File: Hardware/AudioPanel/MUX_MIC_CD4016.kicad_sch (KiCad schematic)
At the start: 8 parts, among them U57 ADG729, U58 ADG729

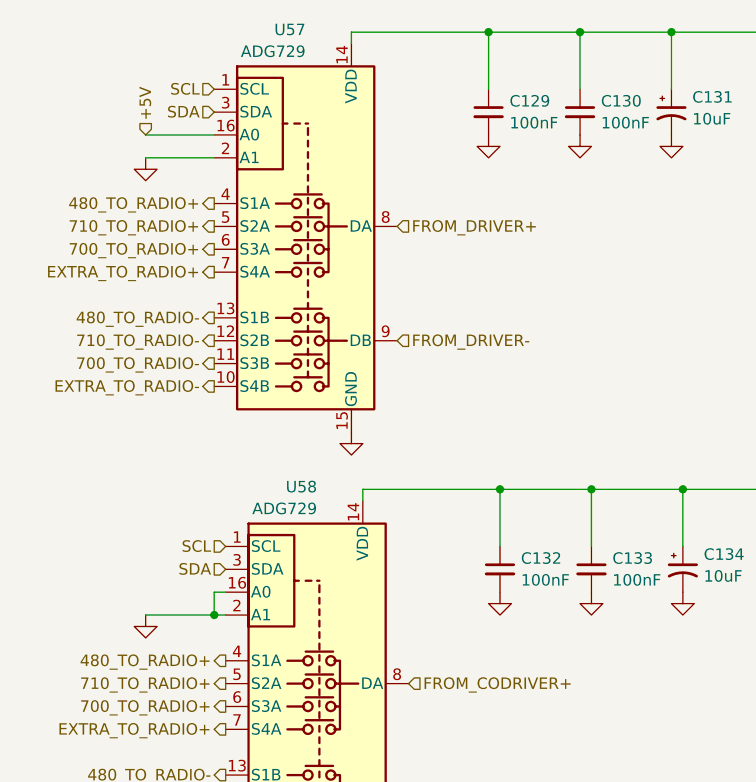
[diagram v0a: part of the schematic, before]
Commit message: Added MIC port protection
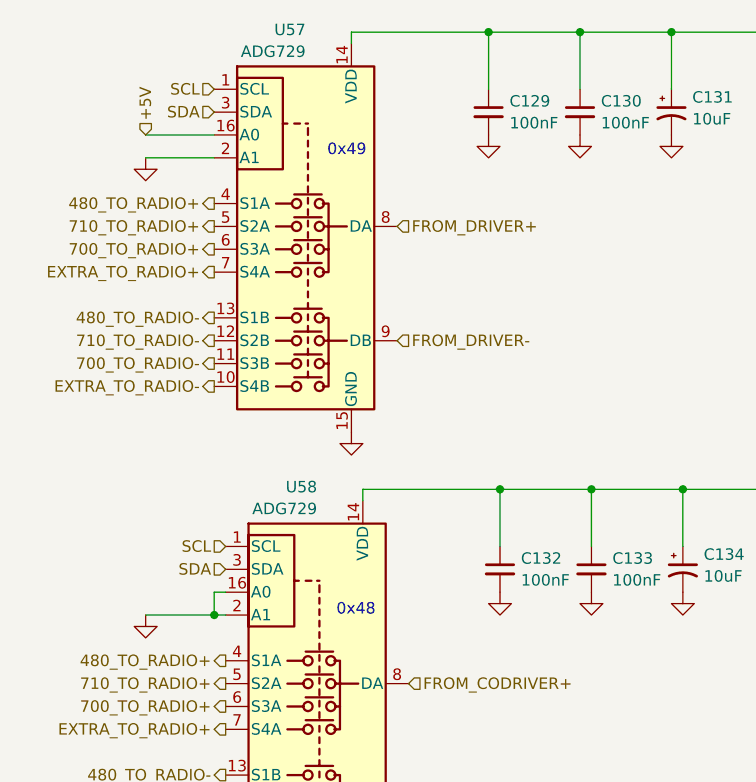
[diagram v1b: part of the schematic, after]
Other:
- note added: "0x48"
- note added: "0x49"
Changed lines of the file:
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@@
 	(generator_version "9.0")
 	(paper "A4")
+	(text "0x48"
+		(exclude_from_sim no)
+		(at 93.218 111.252 0)
+		(effects
+			(font
+				(size 1.27 1.27)
+			)
+		)
+	)
+	(text "0x49"
+		(exclude_from_sim no)
+		(at 92.202 60.198 0)
+		(effects
+			(font
+				(size 1.27 1.27)
+			)
+		)
+	)
 	(junction
 		(at 107.95 46.99)

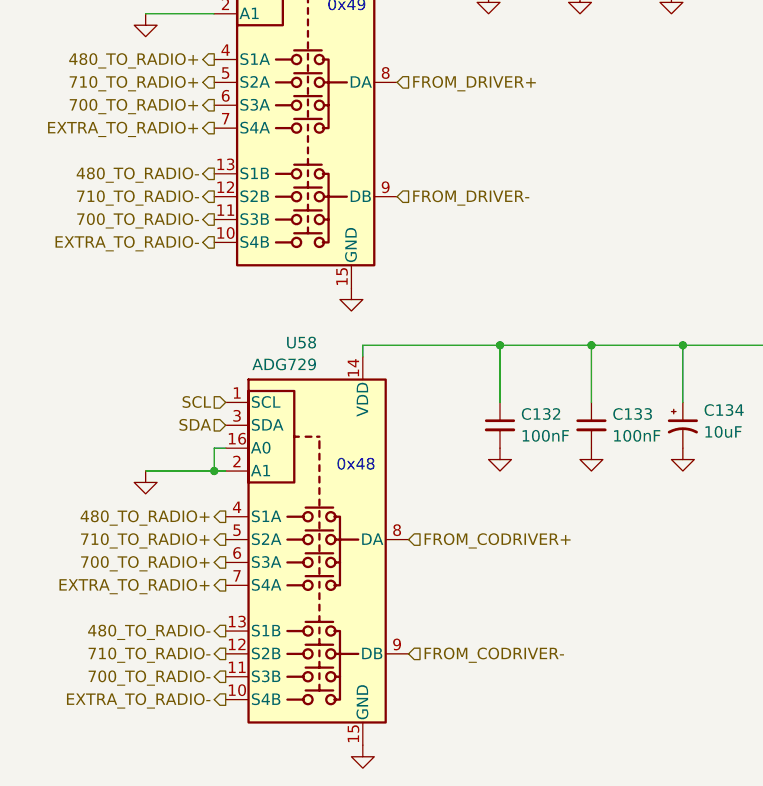
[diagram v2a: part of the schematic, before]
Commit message: Revisiting the audio input buffer circuit
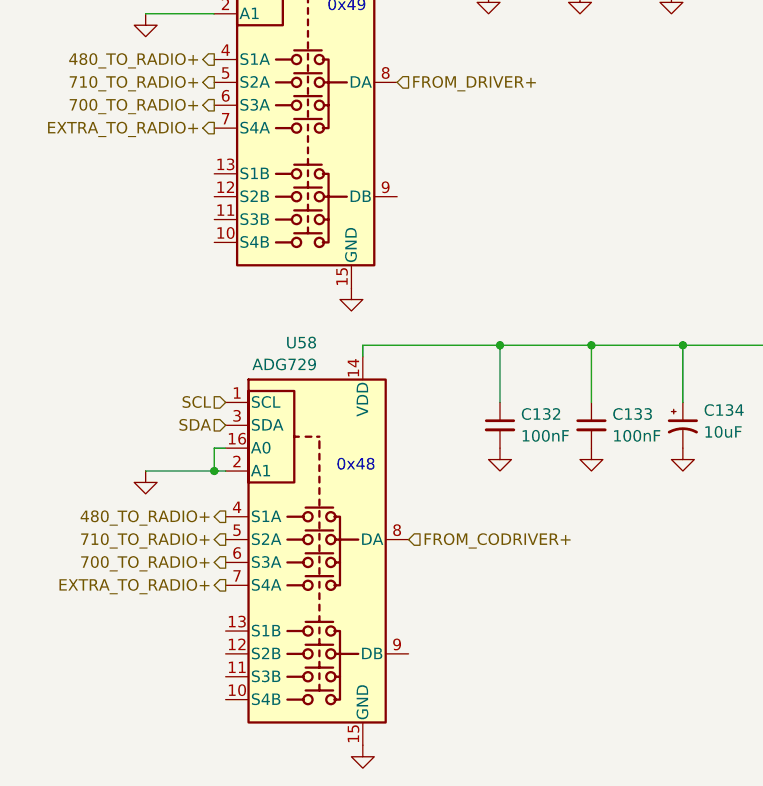
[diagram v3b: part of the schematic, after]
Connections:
- net 480_TO_RADIO-: no longer names the net of U58.13 (S1B)
- net 480_TO_RADIO-: no longer U57.13 (S1B)
- net 700_TO_RADIO-: no longer names the net of U58.11 (S3B)
- net 700_TO_RADIO-: no longer U57.11 (S3B)
- net 710_TO_RADIO-: no longer names the net of U58.12 (S2B)
- net 710_TO_RADIO-: no longer U57.12 (S2B)
- net EXTRA_TO_RADIO-: no longer names the net of U58.10 (S4B)
- net EXTRA_TO_RADIO-: no longer U57.10 (S4B)
- net FROM_CODRIVER-: no longer names the net of U58.9 (DB)
- net FROM_DRIVER-: no longer names the net of U57.9 (DB)
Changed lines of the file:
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@@
-		)
-	)
-	(hierarchical_label "FROM_DRIVER-"
-		(shape input)
-		(at 97.79 81.28 0)
-		(effects
-			(font
-				(size 1.27 1.27)
-			)
-			(justify left)
 		)
 	)
@@
 		)
 	)
-	(hierarchical_label "480_TO_RADIO-"
-		(shape output)
-		(at 77.47 78.74 180)
-		(effects
-			(font
-				(size 1.27 1.27)
-			)
-			(justify right)
-		)
-	)
 	(hierarchical_label "+5V"
 		(shape input)
@@
 		)
 	)
-	(hierarchical_label "710_TO_RADIO-"
-		(shape output)
-		(at 78.74 132.08 180)
-		(effects
-			(font
-				(size 1.27 1.27)
-			)
-			(justify right)
-		)
-	)
-	(hierarchical_label "710_TO_RADIO-"
-		(shape output)
-		(at 77.47 81.28 180)
-		(effects
-			(font
-				(size 1.27 1.27)
-			)
-			(justify right)
-		)
-	)
 	(hierarchical_label "SCL"
 		(shape input)
@@
 			)
 			(justify right)
-		)
-	)
-	(hierarchical_label "700_TO_RADIO-"
-		(shape output)
-		(at 78.74 134.62 180)
-		(effects
-			(font
-				(size 1.27 1.27)
-			)
-			(justify right)
-		)
-	)
-	(hierarchical_label "FROM_CODRIVER-"
-		(shape input)
-		(at 99.06 132.08 0)
-		(effects
-			(font
-				(size 1.27 1.27)
-			)
-			(justify left)
 		)
 	)
@@
 		)
 	)
-	(hierarchical_label "480_TO_RADIO-"
-		(shape output)
-		(at 78.74 129.54 180)
-		(effects
-			(font
-				(size 1.27 1.27)
-			)
-			(justify right)
-		)
-	)
 	(hierarchical_label "FROM_CODRIVER+"
 		(shape input)
@@
 			)
 			(justify left)
-		)
-	)
-	(hierarchical_label "700_TO_RADIO-"
-		(shape output)
-		(at 77.47 83.82 180)
-		(effects
-			(font
-				(size 1.27 1.27)
-			)
-			(justify right)
-		)
-	)
-	(hierarchical_label "EXTRA_TO_RADIO-"
-		(shape output)
-		(at 78.74 137.16 180)
-		(effects
-			(font
-				(size 1.27 1.27)
-			)
-			(justify right)
 		)
 	)
@@
 		)
 	)
-	(hierarchical_label "EXTRA_TO_RADIO-"
-		(shape output)
-		(at 77.47 86.36 180)
-		(effects
-			(font
-				(size 1.27 1.27)
-			)
-			(justify right)
-		)
-	)

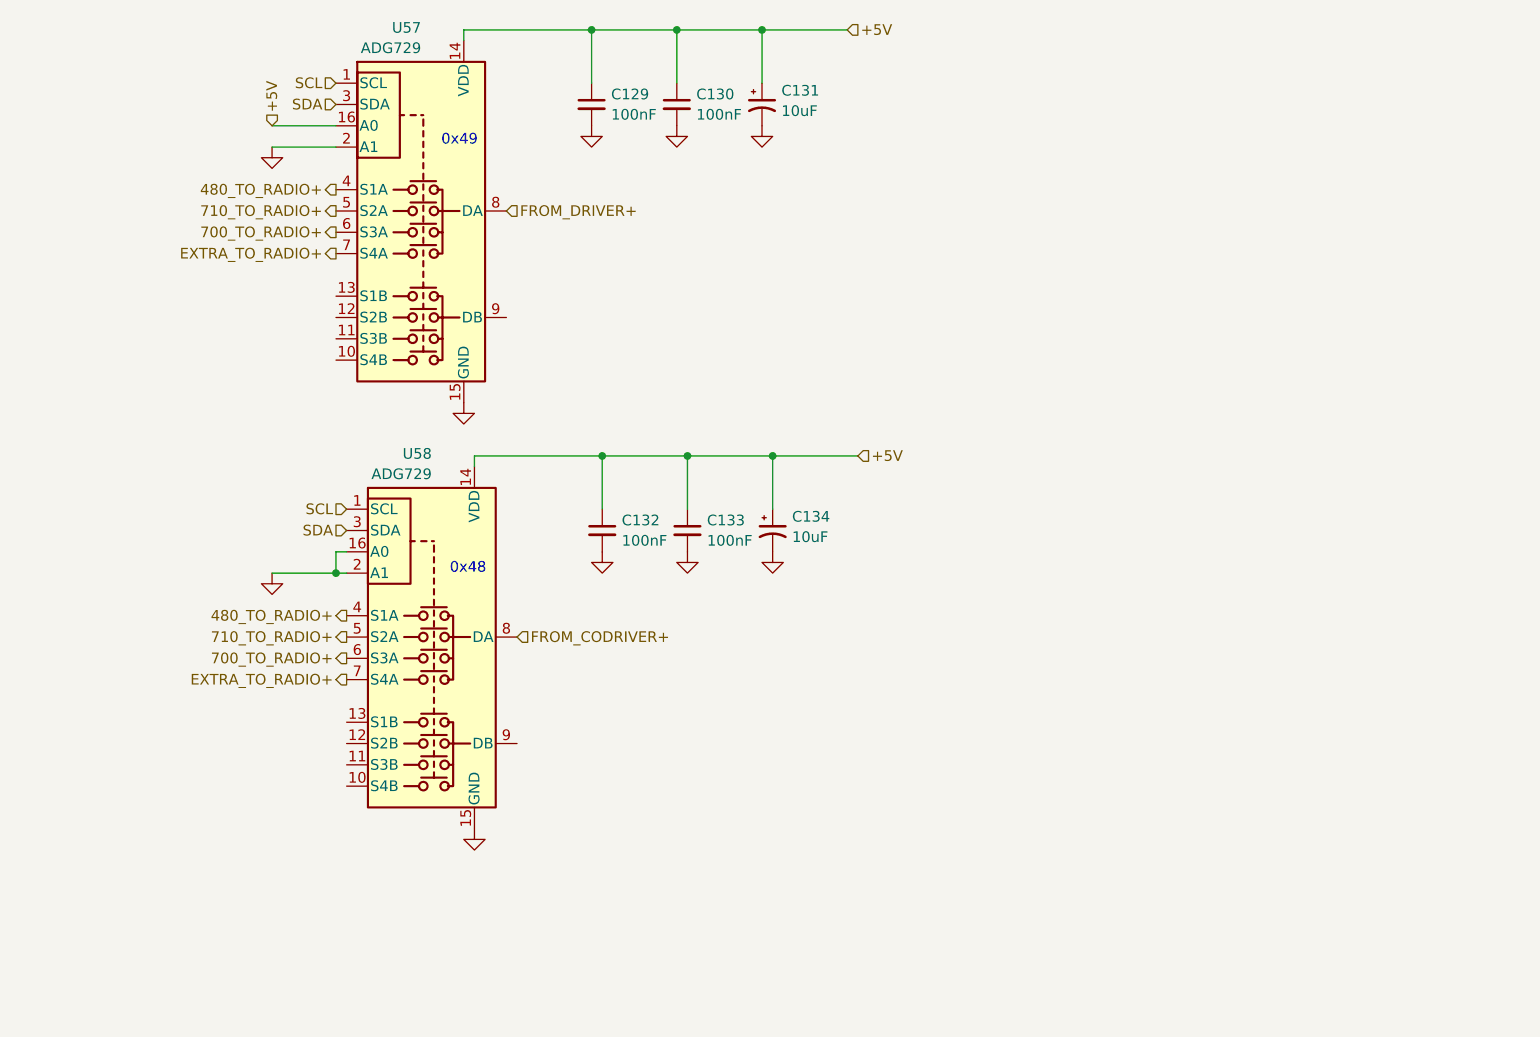
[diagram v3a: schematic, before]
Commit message: Added group labels
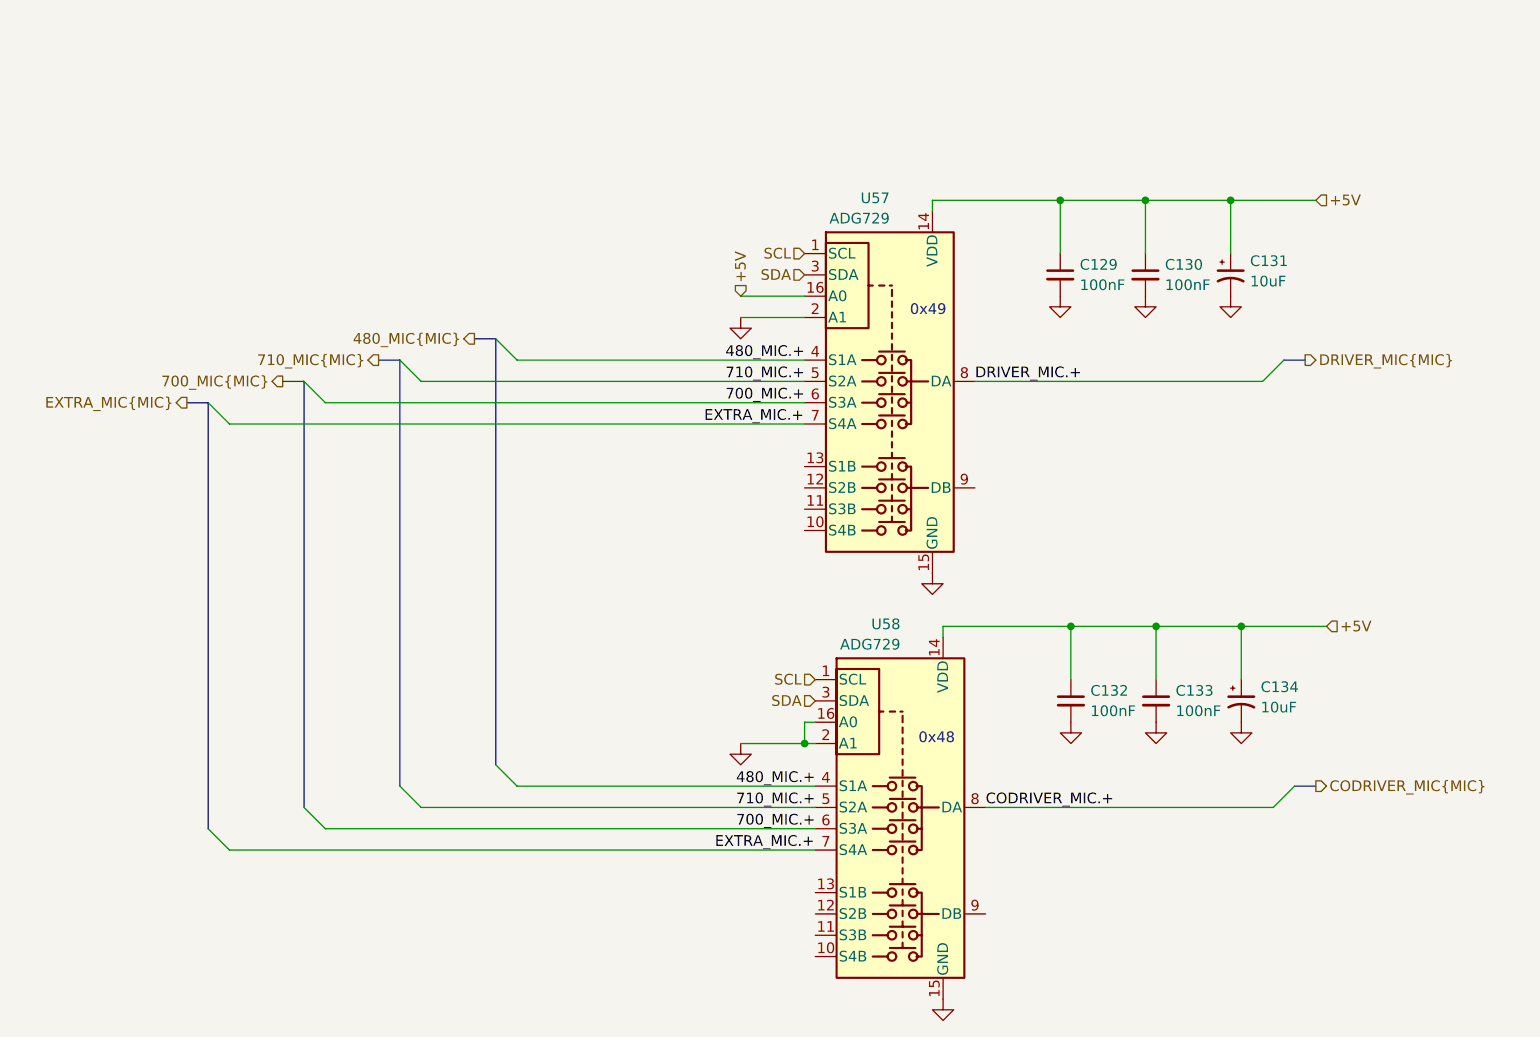
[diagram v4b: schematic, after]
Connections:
- net 480_TO_RADIO+ renamed 480_MIC.+
- net 700_TO_RADIO+ renamed 700_MIC.+
- net 710_TO_RADIO+ renamed 710_MIC.+
- net EXTRA_TO_RADIO+ renamed EXTRA_MIC.+
- net FROM_CODRIVER+ renamed CODRIVER_MIC.+
- net FROM_DRIVER+ renamed DRIVER_MIC.+
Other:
- moved on the sheet: C129, C130, C131, C132, C133, C134, U57, U58
